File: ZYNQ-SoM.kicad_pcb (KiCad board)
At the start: 6 copper layers, 50 x 40 mm, 9 parts, among them J1 AXK500137YG, J2 AXK500137YG, U1 MT41K256M16TW-107_P, U2 W25Q256FVEI, U201 xc7z010clg400

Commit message: feat: finish ddr sch design
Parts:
- added C201: 100n, Capacitor_SMD:C_0402_1005Metric, F.Cu at (105.0, 83.3)
- added C202: 100n, Capacitor_SMD:C_0402_1005Metric, F.Cu at (105.0, 85.3)
- added C203: 100n, Capacitor_SMD:C_0402_1005Metric, F.Cu at (105.0, 87.3)
- added C204: 100n, Capacitor_SMD:C_0402_1005Metric, F.Cu at (105.0, 89.2)
- added C205: 100n, Capacitor_SMD:C_0402_1005Metric, F.Cu at (105.0, 91.2)
- added C206: 100n, Capacitor_SMD:C_0402_1005Metric, F.Cu at (107.9, 83.3)
- added C207: 100n, Capacitor_SMD:C_0402_1005Metric, F.Cu at (94.7, 82.9)
- added C208: 100n, Capacitor_SMD:C_0402_1005Metric, F.Cu at (94.7, 84.9)
- added C209: 100n, Capacitor_SMD:C_0402_1005Metric, F.Cu at (107.9, 89.2)
- added C210: 100n, Capacitor_SMD:C_0402_1005Metric, F.Cu at (107.9, 91.2)
- added C211: 100n, Capacitor_SMD:C_0402_1005Metric, F.Cu at (110.7, 83.3)
- added C212: 100n, Capacitor_SMD:C_0402_1005Metric, F.Cu at (110.7, 85.3)
- added C213: 10n, Capacitor_SMD:C_0402_1005Metric, F.Cu at (129.0, 97.2)
- added C214: 100n, Capacitor_SMD:C_0402_1005Metric, F.Cu at (129.0, 99.2)
- added R201: 240R, Resistor_SMD:R_0402_1005Metric, F.Cu at (94.8, 76.3)
- added R202: 10k, Resistor_SMD:R_0402_1005Metric, F.Cu at (95.7, 69.4)
- added R203: 10k, Resistor_SMD:R_0402_1005Metric, F.Cu at (95.7, 71.4)
- added R204: 80R6, Resistor_SMD:R_0402_1005Metric, F.Cu at (128.3, 91.7)
- added R205: 80R6, Resistor_SMD:R_0402_1005Metric, F.Cu at (128.3, 93.7)
- added R206: 80R6, Resistor_SMD:R_0402_1005Metric, F.Cu at (95.7, 73.1)
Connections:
- U1 pad A1: VDDQ -> +1V5
- U1 pad A2: unconnected-(U1-DQ13-PadA2) -> /DDR3/DDR_D9
- U1 pad A3: unconnected-(U1-DQ15-PadA3) -> /DDR3/DDR_D10
- U1 pad A7: unconnected-(U1-DQ12-PadA7) -> /DDR3/DDR_D13
- U1 pad A8: VDDQ -> +1V5
- U1 pad A9: VSS -> GND
- U1 pad B1: VSSQ -> GND
- U1 pad B2: VDD -> +1V5
- U1 pad B3: VSS -> GND
- U1 pad B7: unconnected-(U1-~{UDQS}-PadB7) -> /DDR3/DDR_DQS1_N
- U1 pad B8: unconnected-(U1-DQ14-PadB8) -> /DDR3/DDR_D15
- U1 pad B9: VSSQ -> GND
- U1 pad C1: VDDQ -> +1V5
- U1 pad C2: unconnected-(U1-DQ11-PadC2) -> /DDR3/DDR_D8
- U1 pad C3: unconnected-(U1-DQ9-PadC3) -> /DDR3/DDR_D11
- U1 pad C7: unconnected-(U1-UDQS-PadC7) -> /DDR3/DDR_DQS1_P
- U1 pad C8: unconnected-(U1-DQ10-PadC8) -> /DDR3/DDR_D12
- U1 pad C9: VDDQ -> +1V5
- U1 pad D1: VSSQ -> GND
- U1 pad D2: VDDQ -> +1V5
- U1 pad D3: unconnected-(U1-UDM-PadD3) -> /DDR3/DDR_DM1
- U1 pad D7: unconnected-(U1-DQ8-PadD7) -> /DDR3/DDR_D14
- U1 pad D8: VSSQ -> GND
- U1 pad D9: VDD -> +1V5
- U1 pad E1: VSS -> GND
- U1 pad E2: VSSQ -> GND
- U1 pad E3: unconnected-(U1-DQ0-PadE3) -> /DDR3/DDR_D2
- U1 pad E7: unconnected-(U1-LDM-PadE7) -> /DDR3/DDR_DM0
- U1 pad E8: VSSQ -> GND
- U1 pad E9: VDDQ -> +1V5
- U1 pad F1: VDDQ -> +1V5
- U1 pad F2: unconnected-(U1-DQ2-PadF2) -> /DDR3/DDR_D0
- U1 pad F3: unconnected-(U1-LDQS-PadF3) -> /DDR3/DDR_DQS0_P
- U1 pad F7: unconnected-(U1-DQ1-PadF7) -> /DDR3/DDR_D7
- U1 pad F8: unconnected-(U1-DQ3-PadF8) -> /DDR3/DDR_D1
- U1 pad F9: VSSQ -> GND
- U1 pad G1: VSSQ -> GND
- U1 pad G2: unconnected-(U1-DQ6-PadG2) -> /DDR3/DDR_D6
- U1 pad G3: unconnected-(U1-~{LDQS}-PadG3) -> /DDR3/DDR_DQS0_N
- U1 pad G7: VDD -> +1V5
- U1 pad G8: VSS -> GND
- U1 pad G9: VSSQ -> GND
- U1 pad H1: unconnected-(U1-VREFDQ-PadH1) -> VTTREF
- U1 pad H2: VDDQ -> +1V5
- U1 pad H3: unconnected-(U1-DQ4-PadH3) -> /DDR3/DDR_D5
- U1 pad H7: unconnected-(U1-DQ7-PadH7) -> /DDR3/DDR_D4
- U1 pad H8: unconnected-(U1-DQ5-PadH8) -> /DDR3/DDR_D3
- U1 pad H9: VDDQ -> +1V5
- U1 pad J2: VSS -> GND
- U1 pad J3: unconnected-(U1-~{RAS}-PadJ3) -> /DDR3/DDR_~{RAS}
- U1 pad J7: unconnected-(U1-CK-PadJ7) -> /DDR3/DDR_CLK_P
- U1 pad J8: VSS -> GND
- U1 pad K1: unconnected-(U1-ODT-PadK1) -> /DDR3/DDR_ODT
- U1 pad K2: VDD -> +1V5
- U1 pad K3: unconnected-(U1-~{CAS}-PadK3) -> /DDR3/DDR_~{CAS}
- U1 pad K7: unconnected-(U1-~{CK}-PadK7) -> /DDR3/DDR_CLK_N
- U1 pad K8: VDD -> +1V5
- U1 pad K9: unconnected-(U1-CKE-PadK9) -> /DDR3/DDR_CKE
- U1 pad L2: unconnected-(U1-~{CS}-PadL2) -> /DDR3/DDR_~{CS}
- U1 pad L3: unconnected-(U1-~{WE}-PadL3) -> /DDR3/DDR_~{WE}
- U1 pad L7: unconnected-(U1-A10/AP-PadL7) -> /DDR3/DDR_A10
- U1 pad L8: unconnected-(U1-ZQ-PadL8) -> Net-(U1-ZQ)
- U1 pad M1: VSS -> GND
- U1 pad M2: unconnected-(U1-BA0-PadM2) -> /DDR3/DDR_BA0
- U1 pad M3: unconnected-(U1-BA2-PadM3) -> /DDR3/DDR_BA2
- U1 pad M8: unconnected-(U1-VREFCA-PadM8) -> VTTREF
- U1 pad M9: VSS -> GND
- U1 pad N1: VDD -> +1V5
- U1 pad N2: unconnected-(U1-A3-PadN2) -> /DDR3/DDR_A3
- U1 pad N3: unconnected-(U1-A0-PadN3) -> /DDR3/DDR_A0
- U1 pad N7: unconnected-(U1-A12/~{BC}-PadN7) -> /DDR3/DDR_A12
- U1 pad N8: unconnected-(U1-BA1-PadN8) -> /DDR3/DDR_BA1
- U1 pad N9: VDD -> +1V5
- U1 pad P1: VSS -> GND
- U1 pad P2: unconnected-(U1-A5-PadP2) -> /DDR3/DDR_A5
- U1 pad P3: unconnected-(U1-A2-PadP3) -> /DDR3/DDR_A2
- U1 pad P7: unconnected-(U1-A1-PadP7) -> /DDR3/DDR_A1
- U1 pad P8: unconnected-(U1-A4-PadP8) -> /DDR3/DDR_A4
- U1 pad P9: VSS -> GND
- U1 pad R1: VDD -> +1V5
- U1 pad R2: unconnected-(U1-A7-PadR2) -> /DDR3/DDR_A7
- U1 pad R3: unconnected-(U1-A9-PadR3) -> /DDR3/DDR_A9
- U1 pad R7: unconnected-(U1-A11-PadR7) -> /DDR3/DDR_A11
- U1 pad R8: unconnected-(U1-A6-PadR8) -> /DDR3/DDR_A6
- U1 pad R9: VDD -> +1V5
- U1 pad T1: VSS -> GND
- U1 pad T2: unconnected-(U1-~{RESET}-PadT2) -> /DDR3/DDR_~{RESET}
- U1 pad T3: unconnected-(U1-A13-PadT3) -> /DDR3/DDR_A13
- U1 pad T7: unconnected-(U1-A14-PadT7) -> /DDR3/DDR_A14
- U1 pad T8: unconnected-(U1-A8-PadT8) -> /DDR3/DDR_A8
- U1 pad T9: VSS -> GND
- U201 pad A1: unconnected-(U201G-PS_DDR_DM0_502-PadA1) -> /DDR3/DDR_DM0
- U201 pad A2: unconnected-(U201G-PS_DDR_DQ2_502-PadA2) -> /DDR3/DDR_D2
- U201 pad A3: Net-(U201G-VCCO_DDR_502[10]-PadA3) -> +1V5
- U201 pad A4: unconnected-(U201G-PS_DDR_DQ3_502-PadA4) -> /DDR3/DDR_D3
- U201 pad B2: unconnected-(U201G-PS_DDR_DQS_N0_502-PadB2) -> /DDR3/DDR_DQS0_N
- U201 pad B3: unconnected-(U201G-PS_DDR_DQ1_502-PadB3) -> /DDR3/DDR_D1
- U201 pad B4: unconnected-(U201G-PS_DDR_DRST_B_502-PadB4) -> /DDR3/DDR_~{RESET}
- U201 pad C1: unconnected-(U201G-PS_DDR_DQ6_502-PadC1) -> /DDR3/DDR_D6
- U201 pad C2: unconnected-(U201G-PS_DDR_DQS_P0_502-PadC2) -> /DDR3/DDR_DQS0_P
- U201 pad C3: unconnected-(U201G-PS_DDR_DQ0_502-PadC3) -> /DDR3/DDR_D0
- U201 pad D1: unconnected-(U201G-PS_DDR_DQ5_502-PadD1) -> /DDR3/DDR_D5
- U201 pad D2: Net-(U201G-VCCO_DDR_502[10]-PadA3) -> +1V5
- U201 pad D3: unconnected-(U201G-PS_DDR_DQ4_502-PadD3) -> /DDR3/DDR_D4
- U201 pad D4: unconnected-(U201G-PS_DDR_A13_502-PadD4) -> /DDR3/DDR_A13
- U201 pad E1: unconnected-(U201G-PS_DDR_DQ7_502-PadE1) -> /DDR3/DDR_D7
- U201 pad E2: unconnected-(U201G-PS_DDR_DQ8_502-PadE2) -> /DDR3/DDR_D8
- U201 pad E3: unconnected-(U201G-PS_DDR_DQ9_502-PadE3) -> /DDR3/DDR_D9
- U201 pad E4: unconnected-(U201G-PS_DDR_A12_502-PadE4) -> /DDR3/DDR_A12
- U201 pad E5: Net-(U201G-VCCO_DDR_502[10]-PadA3) -> +1V5
- U201 pad F1: unconnected-(U201G-PS_DDR_DM1_502-PadF1) -> /DDR3/DDR_DM1
- U201 pad F2: unconnected-(U201G-PS_DDR_DQS_N1_502-PadF2) -> /DDR3/DDR_DQS1_N
- U201 pad F4: unconnected-(U201G-PS_DDR_A14_502-PadF4) -> /DDR3/DDR_A14
- U201 pad F5: unconnected-(U201G-PS_DDR_A10_502-PadF5) -> /DDR3/DDR_A10
- U201 pad G1: Net-(U201G-VCCO_DDR_502[10]-PadA3) -> +1V5
- U201 pad G2: unconnected-(U201G-PS_DDR_DQS_P1_502-PadG2) -> /DDR3/DDR_DQS1_P
- U201 pad G3: unconnected-(U201G-PS_DDR_DQ10_502-PadG3) -> /DDR3/DDR_D10
- U201 pad G4: unconnected-(U201G-PS_DDR_A11_502-PadG4) -> /DDR3/DDR_A11
- U201 pad G5: unconnected-(U201G-PS_DDR_VRN_502-PadG5) -> Net-(U201G-PS_DDR_VRN_502)
- U201 pad H1: unconnected-(U201G-PS_DDR_DQ14_502-PadH1) -> /DDR3/DDR_D14
- U201 pad H2: unconnected-(U201G-PS_DDR_DQ13_502-PadH2) -> /DDR3/DDR_D13
- U201 pad H3: unconnected-(U201G-PS_DDR_DQ11_502-PadH3) -> /DDR3/DDR_D11
- U201 pad H4: Net-(U201G-VCCO_DDR_502[10]-PadA3) -> +1V5
- U201 pad H5: unconnected-(U201G-PS_DDR_VRP_502-PadH5) -> Net-(U201G-PS_DDR_VRP_502)
- U201 pad H6: unconnected-(U201G-PS_DDR_VREF0_502-PadH6) -> VTTREF
- U201 pad J1: unconnected-(U201G-PS_DDR_DQ15_502-PadJ1) -> /DDR3/DDR_D15
- U201 pad J3: unconnected-(U201G-PS_DDR_DQ12_502-PadJ3) -> /DDR3/DDR_D12
- U201 pad J4: unconnected-(U201G-PS_DDR_A9_502-PadJ4) -> /DDR3/DDR_A9
- U201 pad J5: unconnected-(U201G-PS_DDR_BA2_502-PadJ5) -> /DDR3/DDR_BA2
- U201 pad K1: unconnected-(U201G-PS_DDR_A8_502-PadK1) -> /DDR3/DDR_A8
- U201 pad K2: unconnected-(U201G-PS_DDR_A1_502-PadK2) -> /DDR3/DDR_A1
- U201 pad K3: unconnected-(U201G-PS_DDR_A3_502-PadK3) -> /DDR3/DDR_A3
- U201 pad K4: unconnected-(U201G-PS_DDR_A7_502-PadK4) -> /DDR3/DDR_A7
- U201 pad L1: unconnected-(U201G-PS_DDR_A5_502-PadL1) -> /DDR3/DDR_A5
- U201 pad L2: unconnected-(U201G-PS_DDR_CKP_502-PadL2) -> /DDR3/DDR_CLK_N
- U201 pad L3: Net-(U201G-VCCO_DDR_502[10]-PadA3) -> +1V5
- U201 pad L4: unconnected-(U201G-PS_DDR_A6_502-PadL4) -> /DDR3/DDR_A6
- U201 pad L5: unconnected-(U201G-PS_DDR_BA0_502-PadL5) -> /DDR3/DDR_BA0
- U201 pad M2: unconnected-(U201G-PS_DDR_CKN_502-PadM2) -> /DDR3/DDR_CLK_P
- U201 pad M3: unconnected-(U201G-PS_DDR_A2_502-PadM3) -> /DDR3/DDR_A2
- U201 pad M4: unconnected-(U201G-PS_DDR_A4_502-PadM4) -> /DDR3/DDR_A4
- U201 pad M5: unconnected-(U201G-PS_DDR_WE_B_502-PadM5) -> /DDR3/DDR_~{WE}
- U201 pad N1: unconnected-(U201G-PS_DDR_CS_B_502-PadN1) -> /DDR3/DDR_~{CS}
- U201 pad N2: unconnected-(U201G-PS_DDR_A0_502-PadN2) -> /DDR3/DDR_A0
- U201 pad N3: unconnected-(U201G-PS_DDR_CKE_502-PadN3) -> /DDR3/DDR_CKE
- U201 pad N5: unconnected-(U201G-PS_DDR_ODT_502-PadN5) -> /DDR3/DDR_ODT
- U201 pad P2: Net-(U201G-VCCO_DDR_502[10]-PadA3) -> +1V5
- U201 pad P4: unconnected-(U201G-PS_DDR_RAS_B_502-PadP4) -> /DDR3/DDR_~{RAS}
- U201 pad P5: unconnected-(U201G-PS_DDR_CAS_B_502-PadP5) -> /DDR3/DDR_~{CAS}
- U201 pad P6: unconnected-(U201G-PS_DDR_VREF1_502-PadP6) -> VTTREF
- U201 pad R4: unconnected-(U201G-PS_DDR_BA1_502-PadR4) -> /DDR3/DDR_BA1
- U201 pad R5: Net-(U201G-VCCO_DDR_502[10]-PadA3) -> +1V5
- U201 pad U1: Net-(U201G-VCCO_DDR_502[10]-PadA3) -> +1V5
- U201 pad V4: Net-(U201G-VCCO_DDR_502[10]-PadA3) -> +1V5

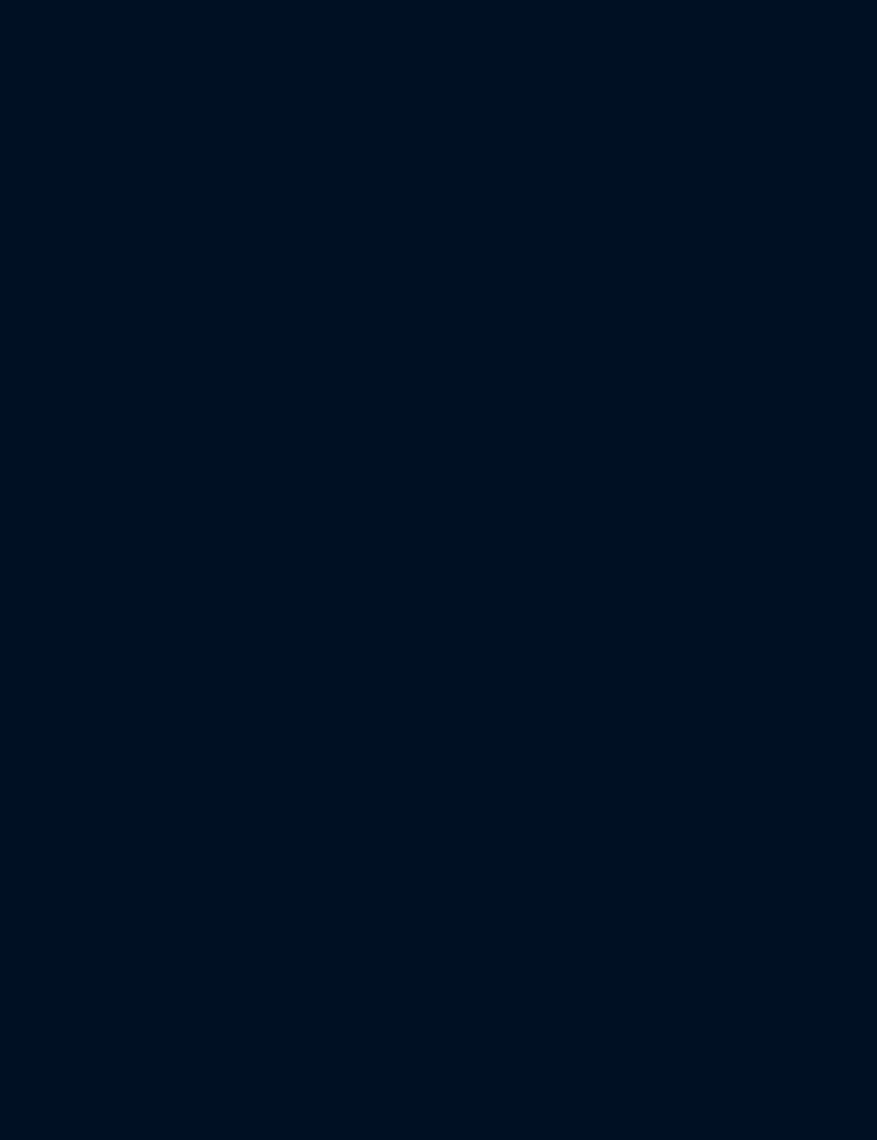
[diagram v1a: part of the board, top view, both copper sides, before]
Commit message: feat: finish power sch design
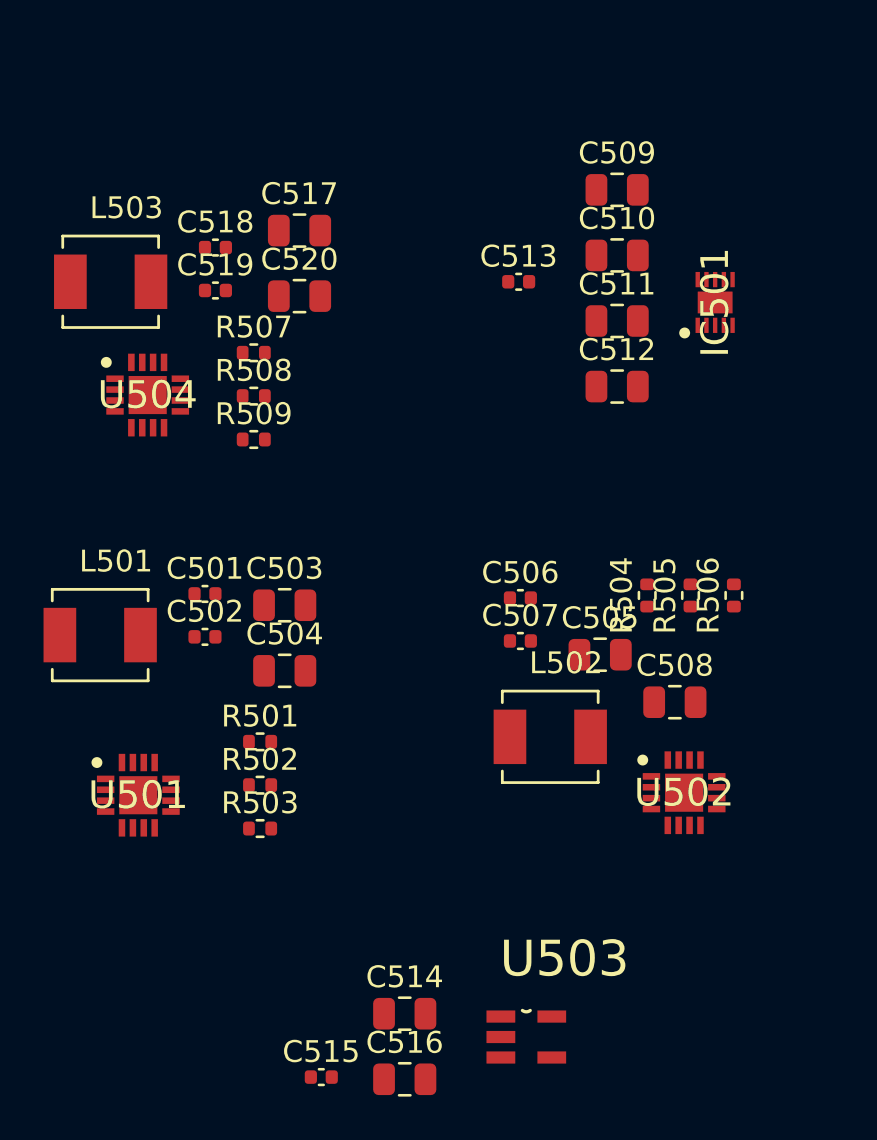
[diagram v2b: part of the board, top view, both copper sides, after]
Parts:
- removed J2: AXK500137YG, Project:AXK500137YG
- added C501: 100n, Capacitor_SMD:C_0402_1005Metric, F.Cu at (49.1, 94.5)
- added C502: 3n3, Capacitor_SMD:C_0402_1005Metric, F.Cu at (49.1, 96.5)
- added C503: 10u, Capacitor_SMD:C_0805_2012Metric, F.Cu at (52.7, 95.0)
- added C504: 22u, Capacitor_SMD:C_0805_2012Metric, F.Cu at (52.7, 98.1)
- added C505: 10u, Capacitor_SMD:C_0805_2012Metric, F.Cu at (67.2, 97.3)
- added C506: 100n, Capacitor_SMD:C_0402_1005Metric, F.Cu at (63.6, 94.7)
- added C507: 3n3, Capacitor_SMD:C_0402_1005Metric, F.Cu at (63.6, 96.7)
- added C508: 22u, Capacitor_SMD:C_0805_2012Metric, F.Cu at (70.7, 99.5)
- added C509: 10u, Capacitor_SMD:C_0805_2012Metric, F.Cu at (68.0, 76.0)
- added C510: 10u, Capacitor_SMD:C_0805_2012Metric, F.Cu at (68.0, 79.0)
- added C511: 10u, Capacitor_SMD:C_0805_2012Metric, F.Cu at (68.0, 82.0)
- added C512: 10u, Capacitor_SMD:C_0805_2012Metric, F.Cu at (68.0, 85.0)
- added C513: 470n, Capacitor_SMD:C_0402_1005Metric, F.Cu at (63.5, 80.2)
- added C514: 10u, Capacitor_SMD:C_0805_2012Metric, F.Cu at (58.2, 113.8)
- added C515: 100n, Capacitor_SMD:C_0402_1005Metric, F.Cu at (54.4, 116.7)
- added C516: 10u, Capacitor_SMD:C_0805_2012Metric, F.Cu at (58.2, 116.8)
- added C517: 10u, Capacitor_SMD:C_0805_2012Metric, F.Cu at (53.4, 77.8)
- added C518: 100n, Capacitor_SMD:C_0402_1005Metric, F.Cu at (49.6, 78.6)
- added C519: 3n3, Capacitor_SMD:C_0402_1005Metric, F.Cu at (49.6, 80.6)
- added C520: 22u, Capacitor_SMD:C_0805_2012Metric, F.Cu at (53.4, 80.9)
- added IC501: TPS51206DSQR, Project:SON40P200X200X80-11N, F.Cu at (72.5, 81.2)
- added J402: AXK500137YG, Project:AXK500137YG, B.Cu at (125.0, 65.5)
- added L501: CMLB041B-2R2MS, Project:IND_CMLB041B-1R0MS, F.Cu at (44.3, 96.4)
- added L502: CMLB041B-2R2MS, Project:IND_CMLB041B-1R0MS, F.Cu at (64.9, 101.1)
- added L503: CMLB041B-2R2MS, Project:IND_CMLB041B-1R0MS, F.Cu at (44.8, 80.2)
- added R501: 100k, Resistor_SMD:R_0402_1005Metric, F.Cu at (51.6, 101.3)
- added R502: 13k, Resistor_SMD:R_0402_1005Metric, F.Cu at (51.6, 103.3)
- added R503: 15k, Resistor_SMD:R_0402_1005Metric, F.Cu at (51.6, 105.3)
- added R504: 100k, Resistor_SMD:R_0402_1005Metric, F.Cu at (69.4, 94.6)
- added R505: 18k7, Resistor_SMD:R_0402_1005Metric, F.Cu at (71.4, 94.6)
- added R506: 15k, Resistor_SMD:R_0402_1005Metric, F.Cu at (73.4, 94.6)
- added R507: 100k, Resistor_SMD:R_0402_1005Metric, F.Cu at (51.3, 83.5)
- added R508: 49.9k, Resistor_SMD:R_0402_1005Metric, F.Cu at (51.3, 85.5)
- added R509: 200k, Resistor_SMD:R_0402_1005Metric, F.Cu at (51.3, 87.4)
- added U501: TPS62130ARGTR, Project:QFN50P300X300X100-17N-D, F.Cu at (46.0, 103.8)
- added U502: TPS62130ARGTR, Project:QFN50P300X300X100-17N-D, F.Cu at (71.1, 103.7)
- added U503: SPX3819M5-L-3-3, Project:SPX3819M5-L-3-3, F.Cu at (63.8, 114.9)
- added U504: TPS62130ARGTR, Project:QFN50P300X300X100-17N-D, F.Cu at (46.5, 85.4)
- renumbered C207 to C301, C208 to C302, C201 to C303, C202 to C304, C203 to C305, C204 to C306, C205 to C307, C206 to C308, C209 to C309, C210 to C310, C213 to C311, C211 to C312, C214 to C313, C212 to C314, H1 to H101, H2 to H102, H3 to H103, H4 to H104, J1 to J401, R201 to R301, R202 to R302, R203 to R303, R206 to R304, R204 to R305, R205 to R306, U201 to U101, U2 to U201, U1 to U301
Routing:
- net unconnected-(J402-Pad84): vias 0 -> 1
- net unconnected-(J402-Pad82): vias 0 -> 1
- net unconnected-(J402-Pad80): vias 0 -> 2
- net unconnected-(J2-Pad84): vias 1 -> 0
- net unconnected-(J2-Pad82): vias 1 -> 0
- net unconnected-(J2-Pad80): vias 2 -> 0

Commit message: feat: continue ps mio sch design
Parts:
- removed U101: xc7z010clg400, Package_BGA:Xilinx_CLG400
- added C201: 470n, Capacitor_SMD:C_0402_1005Metric, F.Cu at (175.6, 92.1)
- added C202: 470n, Capacitor_SMD:C_0402_1005Metric, F.Cu at (175.6, 94.0)
- added C203: 100n, Capacitor_SMD:C_0402_1005Metric, F.Cu at (175.6, 96.0)
- added C507: 10u, Capacitor_SMD:C_0805_2012Metric, F.Cu at (131.8, 108.5)
- added C508: 470n, Capacitor_SMD:C_0402_1005Metric, F.Cu at (139.4, 108.0)
- added C518: 100u, Capacitor_SMD:C_1206_3216Metric, F.Cu at (48.3, 46.6)
- added C520: 470n, Capacitor_SMD:C_0402_1005Metric, F.Cu at (44.0, 47.7)
- added C521: 10u, Capacitor_SMD:C_0805_2012Metric, F.Cu at (53.4, 42.4)
- added C522: 4u7, Capacitor_SMD:C_0603_1608Metric, F.Cu at (51.5, 59.6)
- added C523: 10u, Capacitor_SMD:C_0805_2012Metric, F.Cu at (53.4, 45.4)
- added C524: 4u7, Capacitor_SMD:C_0603_1608Metric, F.Cu at (51.5, 57.1)
- added C525: 4u7, Capacitor_SMD:C_0603_1608Metric, F.Cu at (51.5, 49.6)
- added C526: 470n, Capacitor_SMD:C_0402_1005Metric, F.Cu at (41.2, 49.7)
- added C527: 4u7, Capacitor_SMD:C_0603_1608Metric, F.Cu at (51.5, 52.1)
- added C528: 100n, Capacitor_SMD:C_0402_1005Metric, F.Cu at (44.0, 35.9)
- added C530: 470n, Capacitor_SMD:C_0402_1005Metric, F.Cu at (38.3, 47.7)
- added C532: 470n, Capacitor_SMD:C_0402_1005Metric, F.Cu at (38.3, 49.7)
- added C533: 4u7, Capacitor_SMD:C_0603_1608Metric, F.Cu at (55.5, 49.6)
- added C536: 100n, Capacitor_SMD:C_0402_1005Metric, F.Cu at (41.2, 35.9)
- added C537: 4u7, Capacitor_SMD:C_0603_1608Metric, F.Cu at (55.5, 52.1)
- added C538: 100n, Capacitor_SMD:C_0402_1005Metric, F.Cu at (41.2, 37.9)
- added C539: 470n, Capacitor_SMD:C_0402_1005Metric, F.Cu at (44.0, 37.9)
- added C540: 10u, Capacitor_SMD:C_0805_2012Metric, F.Cu at (53.4, 36.4)
- added C541: 100n, Capacitor_SMD:C_0402_1005Metric, F.Cu at (41.2, 39.8)
- added C542: 100n, Capacitor_SMD:C_0402_1005Metric, F.Cu at (44.0, 39.8)
- added C543: 100u, Capacitor_SMD:C_1206_3216Metric, F.Cu at (48.3, 36.6)
- added C544: 100u, Capacitor_SMD:C_1206_3216Metric, F.Cu at (48.3, 39.9)
- added C545: 100u, Capacitor_SMD:C_1206_3216Metric, F.Cu at (48.3, 43.3)
- added C546: 4u7, Capacitor_SMD:C_0603_1608Metric, F.Cu at (47.5, 57.1)
- added C547: 100n, Capacitor_SMD:C_0402_1005Metric, F.Cu at (41.2, 41.8)
- added C548: 4u7, Capacitor_SMD:C_0603_1608Metric, F.Cu at (47.5, 49.6)
- added C549: 4u7, Capacitor_SMD:C_0603_1608Metric, F.Cu at (47.5, 52.1)
- added C550: 4u7, Capacitor_SMD:C_0603_1608Metric, F.Cu at (47.5, 54.6)
- added C551: 470n, Capacitor_SMD:C_0402_1005Metric, F.Cu at (38.3, 43.8)
- added C552: 100n, Capacitor_SMD:C_0402_1005Metric, F.Cu at (41.2, 43.8)
- added C553: 4u7, Capacitor_SMD:C_0603_1608Metric, F.Cu at (55.5, 54.6)
- added C554: 470n, Capacitor_SMD:C_0402_1005Metric, F.Cu at (35.4, 35.9)
- added C555: 470n, Capacitor_SMD:C_0402_1005Metric, F.Cu at (35.4, 43.8)
- added C556: 470n, Capacitor_SMD:C_0402_1005Metric, F.Cu at (38.3, 35.9)
- added C557: 4u7, Capacitor_SMD:C_0603_1608Metric, F.Cu at (55.5, 57.1)
- added C558: 470n, Capacitor_SMD:C_0402_1005Metric, F.Cu at (35.4, 37.9)
- added C559: 470n, Capacitor_SMD:C_0402_1005Metric, F.Cu at (35.4, 45.7)
- added C560: 470n, Capacitor_SMD:C_0402_1005Metric, F.Cu at (38.3, 37.9)
- added C561: 10u, Capacitor_SMD:C_0805_2012Metric, F.Cu at (53.4, 39.4)
- added C562: 4u7, Capacitor_SMD:C_0603_1608Metric, F.Cu at (51.5, 54.6)
- added C563: 470n, Capacitor_SMD:C_0402_1005Metric, F.Cu at (44.0, 41.8)
- added C564: 470n, Capacitor_SMD:C_0402_1005Metric, F.Cu at (35.4, 39.8)
- added C565: 470n, Capacitor_SMD:C_0402_1005Metric, F.Cu at (35.4, 47.7)
- added C566: 470n, Capacitor_SMD:C_0402_1005Metric, F.Cu at (38.3, 39.8)
- added C567: 4u7, Capacitor_SMD:C_0603_1608Metric, F.Cu at (47.5, 59.6)
- added C568: 470n, Capacitor_SMD:C_0402_1005Metric, F.Cu at (41.2, 45.7)
- added C569: 470n, Capacitor_SMD:C_0402_1005Metric, F.Cu at (44.0, 45.7)
- added C570: 470n, Capacitor_SMD:C_0402_1005Metric, F.Cu at (35.4, 41.8)
- added C571: 470n, Capacitor_SMD:C_0402_1005Metric, F.Cu at (35.4, 49.7)
- added C572: 470n, Capacitor_SMD:C_0402_1005Metric, F.Cu at (38.3, 41.8)
- added C573: 470n, Capacitor_SMD:C_0402_1005Metric, F.Cu at (38.3, 45.7)
- added C574: 100n, Capacitor_SMD:C_0402_1005Metric, F.Cu at (41.2, 47.7)
- added C575: 100n, Capacitor_SMD:C_0402_1005Metric, F.Cu at (44.0, 43.8)
- added D201: LED, LED_SMD:LED_0603_1608Metric, F.Cu at (156.1, 96.0)
- added FB201: 120OHM@100M, Inductor_SMD:L_0603_1608Metric, F.Cu at (160.2, 96.0)
- added FB501: 120OHM@100M, Inductor_SMD:L_0603_1608Metric, F.Cu at (136.0, 108.2)
- added Q201: MMBT3904, Package_TO_SOT_SMD:SOT-23, F.Cu at (176.6, 88.9)
- added R201: 1k, Resistor_SMD:R_0402_1005Metric, F.Cu at (175.6, 75.7)
- added R202: 4k7, Resistor_SMD:R_0402_1005Metric, F.Cu at (175.6, 77.7)
- added R203: 4k7, Resistor_SMD:R_0402_1005Metric, F.Cu at (175.6, 79.7)
- added R204: 330R, Resistor_SMD:R_0402_1005Metric, F.Cu at (175.6, 81.7)
- added R205: 1k, Resistor_SMD:R_0402_1005Metric, F.Cu at (175.6, 83.7)
- added R206: 470R, Resistor_SMD:R_0402_1005Metric, F.Cu at (175.6, 85.6)
- added R207: 20k, Resistor_SMD:R_0402_1005Metric, F.Cu at (178.5, 75.7)
- added R208: 20k, Resistor_SMD:R_0402_1005Metric, F.Cu at (178.5, 77.7)
- added R209: 20k, Resistor_SMD:R_0402_1005Metric, F.Cu at (178.5, 79.7)
- added R210: 20k, Resistor_SMD:R_0402_1005Metric, F.Cu at (178.5, 81.7)
- added R211: 20k, Resistor_SMD:R_0402_1005Metric, F.Cu at (178.5, 83.7)
- added U201: xc7z010clg400, Package_BGA:Xilinx_CLG400, F.Cu at (132.5, 80.0)
- moved C501 69.9 mm to (115.6, 109.8)
- moved C503 69.9 mm to (111.7, 110.6)
- moved C505 69.9 mm to (111.7, 112.6)
- moved C510 69.9 mm to (115.6, 112.9)
- moved L501 69.9 mm to (106.9, 112.2)
- moved R501 69.9 mm to (113.5, 115.5)
- moved R503 69.9 mm to (113.5, 117.5)
- moved R504 69.9 mm to (113.5, 119.4)
- moved U501 69.9 mm to (108.6, 117.4)
- renumbered C517 to C501, C503 to C502, C518 to C503, C501 to C504, C519 to C505, C502 to C506, C514 to C509, C520 to C510, C504 to C511, C505 to C512, C509 to C513, C506 to C514, C510 to C515, C507 to C516, C515 to C517, C516 to C519, C511 to C529, C512 to C531, C508 to C534, C513 to C535, L503 to L501, L501 to L502, L502 to L503, R507 to R501, R501 to R502, R508 to R503, R509 to R504, R502 to R505, R503 to R506, R504 to R507, R505 to R508, R506 to R509, U201 to U202, U504 to U501, U501 to U502, U502 to U504
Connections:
- U202 pad 1: unconnected-(U201-/CS-Pad1) -> QSPI_CS
- U202 pad 2: unconnected-(U201-D0(IO1)-Pad2) -> QSPI_D1
- U202 pad 3: unconnected-(U201-/WP(IO2)-Pad3) -> QSPI_D2_PS_MIO4
- U202 pad 4: unconnected-(U201-GND-Pad4) -> GND
- U202 pad 5: unconnected-(U201-DI(IO0)-Pad5) -> QSPI_D0
- U202 pad 6: unconnected-(U201-CLK-Pad6) -> QSPI_CLK
- U202 pad 7: unconnected-(U201-/HOLD(IO3)-Pad7) -> QSPI_D3_PS_MIO5
- U202 pad 8: unconnected-(U201-VCC-Pad8) -> +3V3
